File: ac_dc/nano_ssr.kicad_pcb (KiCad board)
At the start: 2 copper layers, 134.6 x 77.5 mm, 63 parts, among them K1 CONN_3, K2 CONN_3, M1 VAL**, M2 VAL**, M3 VAL**, M4 VAL**, P1 CONN_5_CUSTOM, P10 2X_BLOCK_CONN, P11 2X_BLOCK_CONN, P12 2X_BLOCK_CONN, P2 CONN_5X2, P3 CONN_4, P4 CONN_2, P5 2X_BLOCK_CONN, P6 2X_BLOCK_CONN, P7 2X_BLOCK_CONN, P8 2X_BLOCK_CONN, P9 2X_BLOCK_CONN, T1 TVS, T2 TVS, T3 TVS, T4 TVS, T5 TVS, T6 TVS, T7 TVS, T8 TVS, U1 ARDUINO_NANO, U2 SSR_DC_6PIN, U3 SSR_DC_6PIN, U4 SSR_DC_6PIN, U5 SSR_DC_6PIN, U6 SSR_DC_6PIN, U7 SSR_DC_6PIN, U8 SSR_DC_6PIN, U9 SSR_DC_6PIN

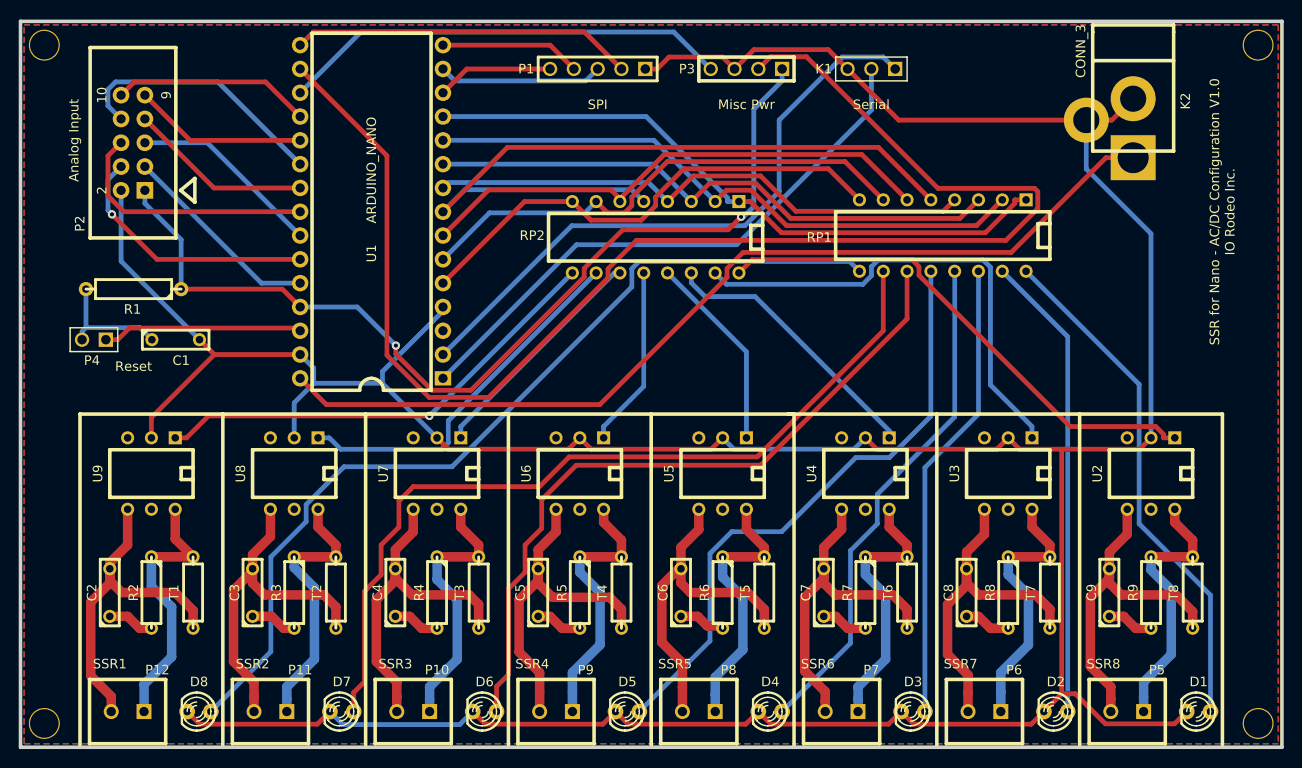
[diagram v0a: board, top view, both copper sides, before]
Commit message: Fixed issure with led pads. Added additional anotation to sild screen.
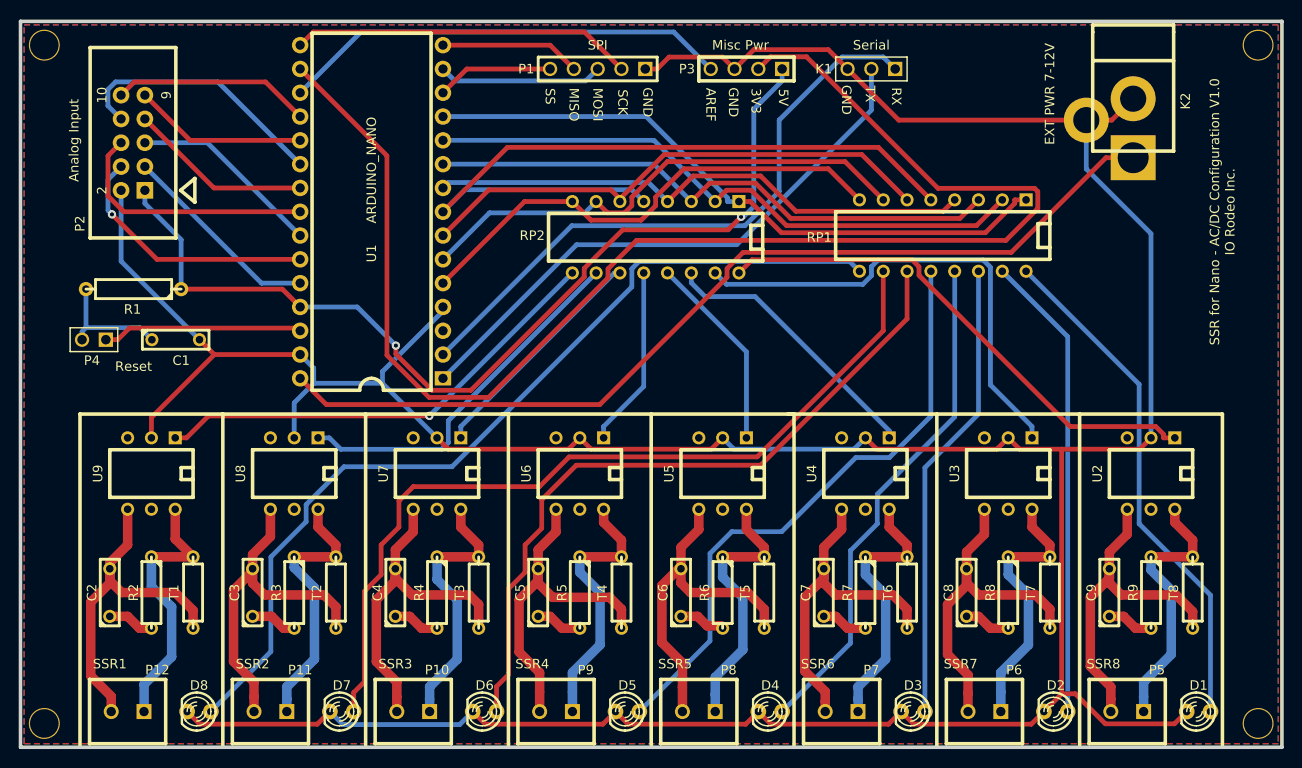
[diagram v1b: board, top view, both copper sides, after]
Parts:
- D1, D2, D3, D4, D5, D6, D7, D8: footprint LED-3MM -> LED-3MM-custom
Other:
- board text added: "3V3"
- board text added: "5V"
- board text added: "AREF"
- board text added: "EXT PWR 7-12V"
- board text added: "GND"
- board text added: "MISO"
- board text added: "MOSI"
- board text added: "RX"
- board text added: "SCK"
- board text added: "SS"
- board text added: "TX"

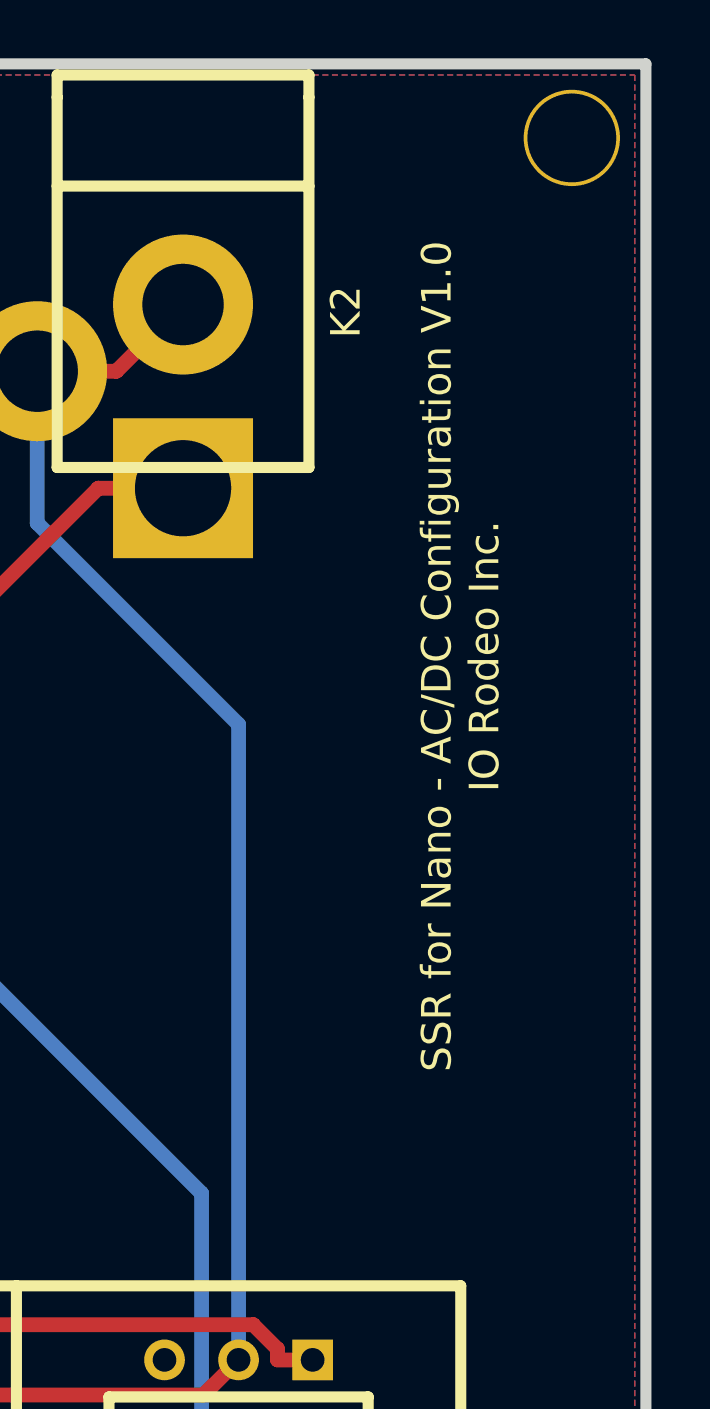
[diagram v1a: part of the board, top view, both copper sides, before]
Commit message: Created v1.1 and new gerber files for ac_dc version.  Modified filled zones slightly - decreased spoke length.
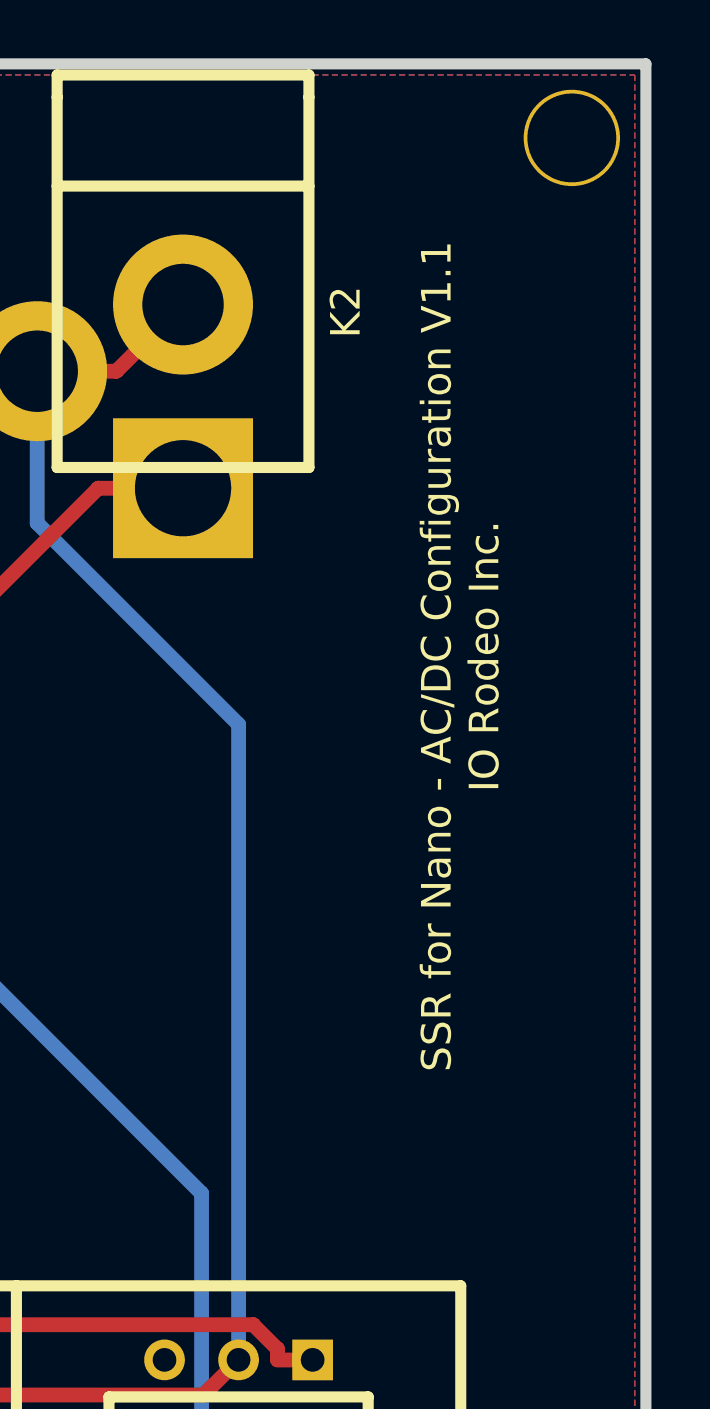
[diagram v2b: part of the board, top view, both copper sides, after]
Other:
- board text added: "SSR for Nano - AC/DC Configuration V1.1 IO Rodeo Inc."
- board text removed: "SSR for Nano - AC/DC Configuration V1.0 IO Rodeo Inc."
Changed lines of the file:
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@@
-(kicad_pcb (version 3) (host pcbnew "(2013-mar-13)-testing")
+(kicad_pcb (version 3) (host pcbnew "(2013-jul-07)-stable")
   (general
     (links 135)
@@
   )
   (page A4)
-  (title_block
-    (date "14 feb 2012")
-  )
   (layers
     (15 Component signal)
@@
       (drillshape 0)
       (scaleselection 1)
-      (outputdirectory gerber_v1p0/))
+      (outputdirectory gerber_v1p1/))
   )
   (net 0 "")
@@
     )
     (fp_text value CONN_4 (at 1.27 2.54 180) (layer F.SilkS) hide
-      (effects (font (thickness 0.3048)))
+      (effects (font (size 1.524 1.524) (thickness 0.3048)))
     )
     (fp_line (start -5.08 -1.27) (end -5.08 1.27) (layer F.SilkS) (width 0.381))
@@
     )
     (fp_text value CONN_5X2 (at 0 6.096 90) (layer F.SilkS) hide
-      (effects (font (thickness 0.3048)))
+      (effects (font (size 1.524 1.524) (thickness 0.3048)))
     )
     (fp_line (start -10.16 -4.572) (end -10.16 4.572) (layer F.SilkS) (width 0.381))
@@
     )
     (fp_text value 2X_BLOCK_CONN (at 0.508 -5.588 180) (layer F.SilkS) hide
-      (effects (font (thickness 0.3048)))
+      (effects (font (size 1.524 1.524) (thickness 0.3048)))
     )
     (fp_line (start -4.064 -3.429) (end -4.064 3.429) (layer F.SilkS) (width 0.381))
@@
     )
     (fp_text value 2X_BLOCK_CONN (at 0.508 -5.588 180) (layer F.SilkS) hide
-      (effects (font (thickness 0.3048)))
+      (effects (font (size 1.524 1.524) (thickness 0.3048)))
     )
     (fp_line (start -4.064 -3.429) (end -4.064 3.429) (layer F.SilkS) (width 0.381))
@@
     )
     (fp_text value 2X_BLOCK_CONN (at 0.508 -5.588 180) (layer F.SilkS) hide
-      (effects (font (thickness 0.3048)))
+      (effects (font (size 1.524 1.524) (thickness 0.3048)))
     )
     (fp_line (start -4.064 -3.429) (end -4.064 3.429) (layer F.SilkS) (width 0.381))
@@
     )
     (fp_text value 2X_BLOCK_CONN (at 0.508 -5.588 180) (layer F.SilkS) hide
-      (effects (font (thickness 0.3048)))
+      (effects (font (size 1.524 1.524) (thickness 0.3048)))
     )
     (fp_line (start -4.064 -3.429) (end -4.064 3.429) (layer F.SilkS) (width 0.381))
@@
     )
     (fp_text value 2X_BLOCK_CONN (at 0.508 -5.588 180) (layer F.SilkS) hide
-      (effects (font (thickness 0.3048)))
+      (effects (font (size 1.524 1.524) (thickness 0.3048)))
     )
     (fp_line (start -4.064 -3.429) (end -4.064 3.429) (layer F.SilkS) (width 0.381))
@@
     )
     (fp_text value 2X_BLOCK_CONN (at 0.508 -5.588 180) (layer F.SilkS) hide
-      (effects (font (thickness 0.3048)))
+      (effects (font (size 1.524 1.524) (thickness 0.3048)))
     )
     (fp_line (start -4.064 -3.429) (end -4.064 3.429) (layer F.SilkS) (width 0.381))
@@
     )
     (fp_text value 2X_BLOCK_CONN (at 0.508 -5.588 180) (layer F.SilkS) hide
-      (effects (font (thickness 0.3048)))
+      (effects (font (size 1.524 1.524) (thickness 0.3048)))
     )
     (fp_line (start -4.064 -3.429) (end -4.064 3.429) (layer F.SilkS) (width 0.381))
@@
     )
     (fp_text value 2X_BLOCK_CONN (at 0.508 -5.588 180) (layer F.SilkS) hide
-      (effects (font (thickness 0.3048)))
+      (effects (font (size 1.524 1.524) (thickness 0.3048)))
     )
     (fp_line (start -4.064 -3.429) (end -4.064 3.429) (layer F.SilkS) (width 0.381))
@@
     (effects (font (size 1.016 1.016) (thickness 0.2032)))
   )
-  (gr_text "SSR for Nano - AC/DC Configuration V1.0\nIO Rodeo Inc. " (at 203.835 69.85 90) (layer F.SilkS)
+  (gr_text "SSR for Nano - AC/DC Configuration V1.1\nIO Rodeo Inc. " (at 203.835 69.85 90) (layer F.SilkS)
     (effects (font (size 1.016 1.016) (thickness 0.2032)))
   )
@@
     (connect_pads (clearance 0.508))
     (min_thickness 0.254)
-    (fill (arc_segments 16) (thermal_gap 2.54) (thermal_bridge_width 2.794))
+    (fill (arc_segments 16) (thermal_gap 0.762) (thermal_bridge_width 0.508))
     (polygon
       (pts
@@
     (connect_pads (clearance 0.508))
     (min_thickness 0.254)
-    (fill (arc_segments 16) (thermal_gap 2.54) (thermal_bridge_width 2.794))
+    (fill (arc_segments 16) (thermal_gap 0.762) (thermal_bridge_width 0.508))
     (polygon
       (pts
